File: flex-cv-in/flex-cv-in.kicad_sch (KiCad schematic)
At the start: 19 parts, among them J1 3.5mm_Mono_Switched, J2 HDR, U1 TLV9061xDBV

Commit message: Update to final Rev. A
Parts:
- added TP1: TP_VREF, TestPoint:TestPoint_Loop_D2.50mm_Drill1.0mm_LowProfile, symbol Connector:TestPoint
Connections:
- net VREF_1.65V: now also TP1.1
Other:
- moved on the sheet: C1, C2, C4, R5, R6

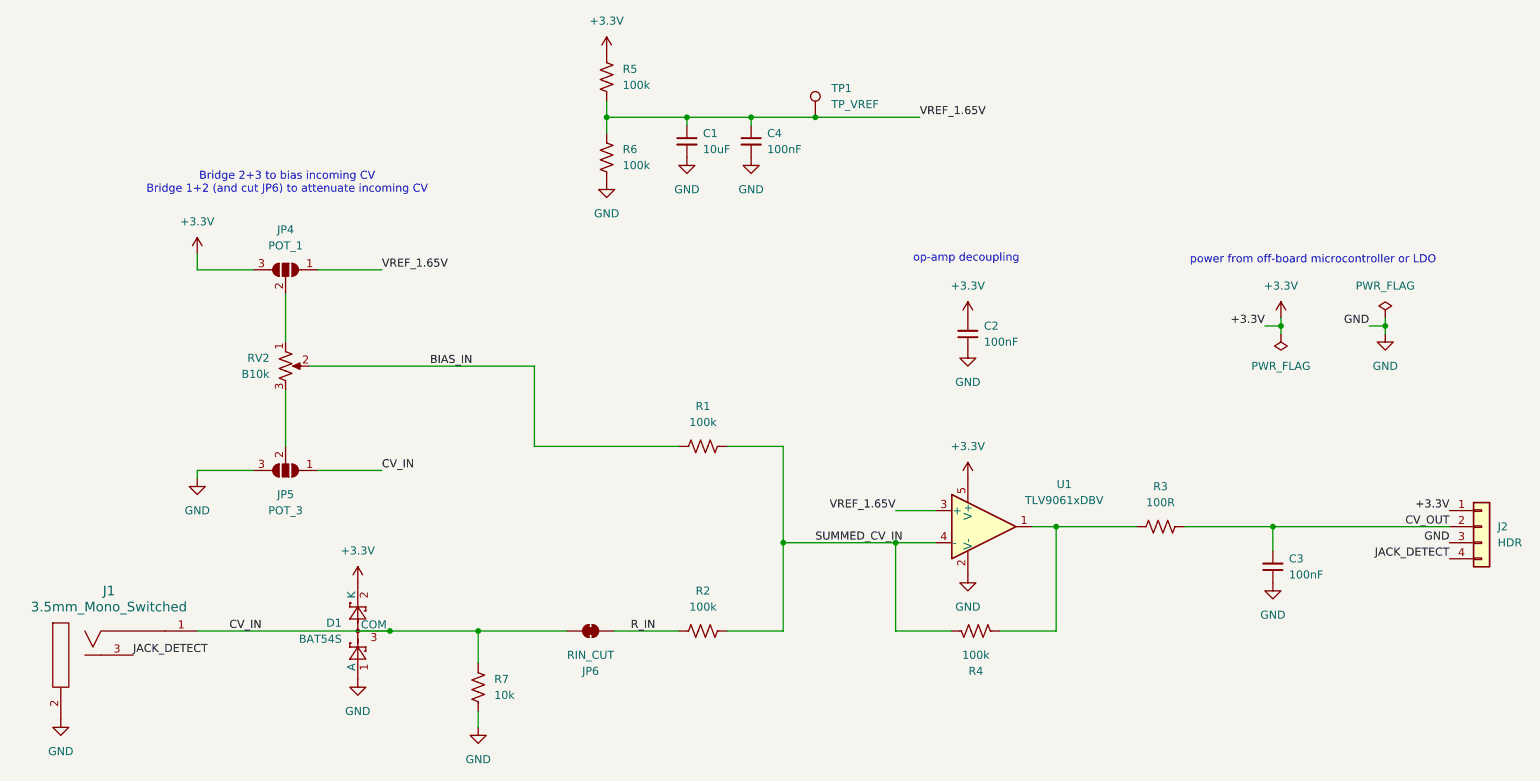
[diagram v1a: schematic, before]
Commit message: flex-cv-in rev. B
Updates and bug fixes:

- Removed jack detect
- Changed R7 connection from GND to VREF_1.65V
- Connected JP5 pad 2 to RV2 pad 3
- Adjusted layout of JP6 to avoid inadvertently cutting CV_IN trace
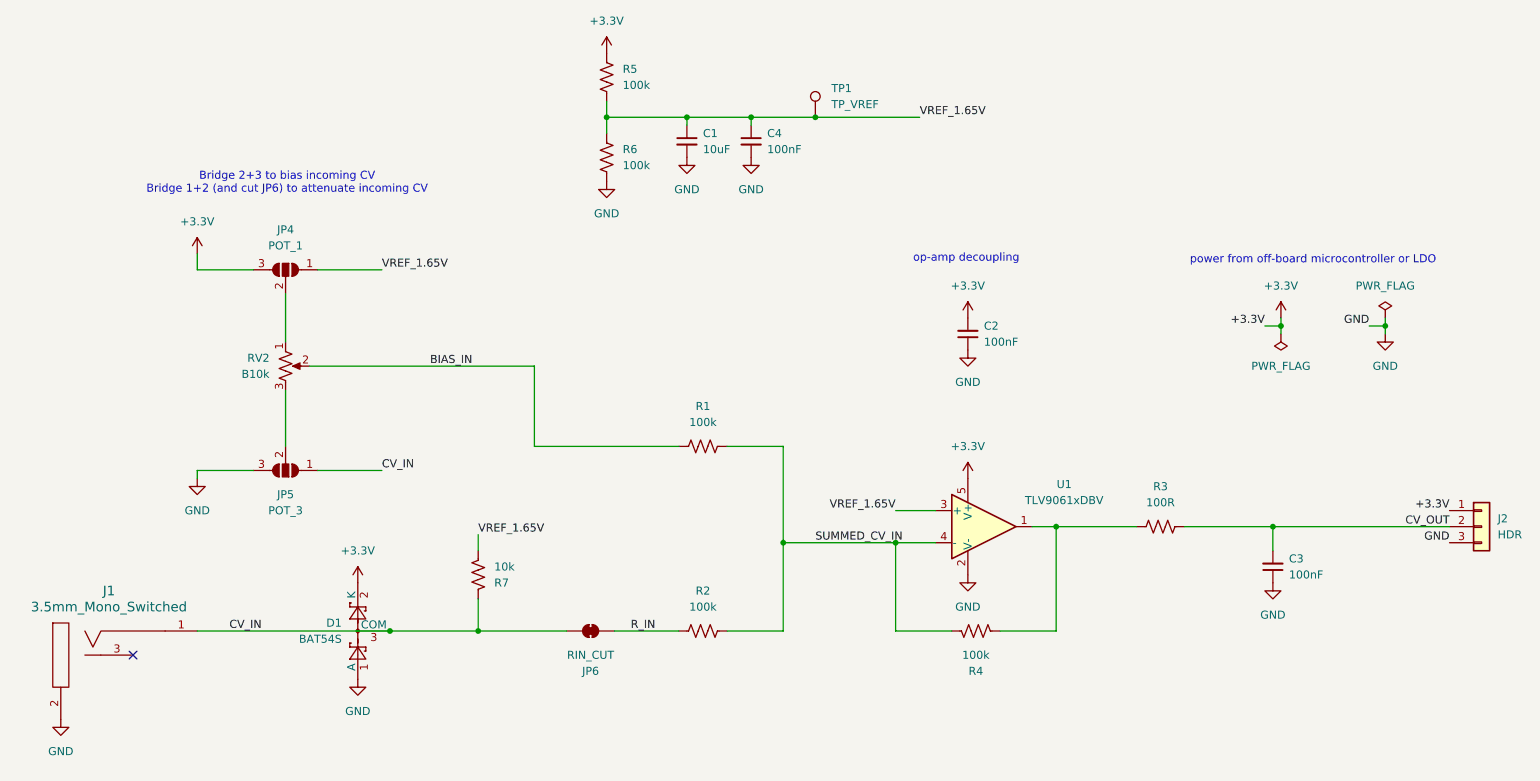
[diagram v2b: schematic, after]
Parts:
- removed J2: HDR, Connector_PinHeader_2.54mm:PinHeader_1x04_P2.54mm_Vertical, symbol Connector_Generic:Conn_01x04
- added J2: HDR, Connector_PinSocket_2.54mm:PinSocket_1x03_P2.54mm_Vertical, symbol Connector_Generic:Conn_01x03
- TP1: footprint TestPoint:TestPoint_Loop_D2.50mm_Drill1.0mm_LowProfile -> TestPoint:TestPoint_Pad_D1.5mm
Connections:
- net +3.3V: now also J2.1 (Pin_1)
- net CV_OUT: now also J2.2 (Pin_2)
- net GND: now also J2.3 (Pin_3); no longer R7.1
- net VREF_1.65V: now also R7.1
- net JACK_DETECT: no longer names the net of J1.3 (SW)
- no-connect marks 0 -> 1
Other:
- moved on the sheet: R7
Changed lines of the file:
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@@
 		(title "patch_bits/flex-cv-in")
 		(date "2025-07-18")
-		(rev "A")
+		(rev "B")
 		(company "Brian Varren")
 	)
@@
 		(color 0 0 0 0)
 	)
+	(no_connect
+		(at 59.69 121.92)
+	)
 	(wire
 		(pts
@@
 	(wire
 		(pts
-			(xy 114.3 130.81) (xy 114.3 133.35)
+			(xy 114.3 105.41) (xy 114.3 102.87)
 		)
 		(stroke
@@
 	(wire
 		(pts
-			(xy 114.3 118.11) (xy 114.3 123.19)
+			(xy 114.3 118.11) (xy 114.3 113.03)
 		)
 		(stroke
@@
 		)
 	)
-	(label "JACK_DETECT"
-		(at 267.97 106.68 180)
-		(effects
-			(font
-				(size 1.27 1.27)
-			)
-			(justify right bottom)
-		)
-	)
 	(label "GND"
 		(at 267.97 104.14 180)
@@
 		)
 	)
+	(label "VREF_1.65V"
+		(at 114.3 102.87 0)
+		(effects
+			(font
+				(size 1.27 1.27)
+			)
+			(justify left bottom)
+		)
+	)
 	(label "GND"
 		(at 255.27 69.85 180)
@@
 		)
 	)
-	(label "JACK_DETECT"
-		(at 59.69 121.92 0)
-		(effects
-			(font
-				(size 1.27 1.27)
-			)
-			(justify left bottom)
-		)
-	)
 	(label "CV_IN"
 		(at 99.06 92.71 0)
@@
 			)
 		)
-		(property "Footprint" "TestPoint:TestPoint_Loop_D2.50mm_Drill1.0mm_LowProfile"
+		(property "Footprint" "TestPoint:TestPoint_Pad_D1.5mm"
 			(at 172.72 36.83 0)
 			(effects
@@
 	(symbol
 		(lib_id "Device:R_US")
-		(at 114.3 127 180)
-		(unit 1)
-		(exclude_from_sim no)
-		(in_bom yes)
-		(on_board yes)
-		(dnp no)
-		(fields_autoplaced yes)
+		(at 114.3 109.22 0)
+		(mirror y)
+		(unit 1)
+		(exclude_from_sim no)
+		(in_bom yes)
+		(on_board yes)
+		(dnp no)
 		(property "Reference" "R7"
-			(at 116.84 125.7299 0)
+			(at 116.84 110.4901 0)
 			(effects
 				(font
@@
 		)
 		(property "Value" "10k"
-			(at 116.84 128.2699 0)
+			(at 116.84 107.9501 0)
 			(effects
 				(font
@@
 		)
 		(property "Footprint" "Resistor_SMD:R_0805_2012Metric"
-			(at 113.284 126.746 90)
+			(at 113.284 109.474 90)
 			(effects
 				(font
@@
 		)
 		(property "Datasheet" "~"
-			(at 114.3 127 0)
+			(at 114.3 109.22 0)
 			(effects
 				(font
@@
 		)
 		(property "Description" "Resistor, US symbol"
-			(at 114.3 127 0)
+			(at 114.3 109.22 0)
 			(effects
 				(font
@@
 	(symbol
 		(lib_id "power:GND")
-		(at 114.3 133.35 0)
-		(unit 1)
-		(exclude_from_sim no)
-		(in_bom yes)
-		(on_board yes)
-		(dnp no)
-		(fields_autoplaced yes)
-		(property "Reference" "#PWR04"
-			(at 114.3 139.7 0)
-			(effects
-				(font
-					(size 1.27 1.27)
-				)
-				(hide yes)
-			)
-		)
-		(property "Value" "GND"
-			(at 114.3 138.43 0)
-			(effects
-				(font
-					(size 1.27 1.27)
-				)
-			)
-		)
-		(property "Footprint" ""
-			(at 114.3 133.35 0)
-			(effects
-				(font
-					(size 1.27 1.27)
-				)
-				(hide yes)
-			)
-		)
-		(property "Datasheet" ""
-			(at 114.3 133.35 0)
-			(effects
-				(font
-					(size 1.27 1.27)
-				)
-				(hide yes)
-			)
-		)
-		(property "Description" "Power symbol creates a global label with name \"GND\" , ground"
-			(at 114.3 133.35 0)
-			(effects
-				(font
-					(size 1.27 1.27)
-				)
-				(hide yes)
-			)
-		)
-		(pin "1"
-		)
-		(instances
-			(project ""
-				(path "/9d06852e-8604-41db-99eb-9a7a414e7408"
-					(reference "#PWR04")
-					(unit 1)
-				)
-			)
-		)
-	)
-	(symbol
-		(lib_id "power:GND")
 		(at 157.48 43.18 0)
 		(unit 1)
@@
 	)
 	(symbol
-		(lib_id "Connector_Generic:Conn_01x04")
-		(at 273.05 101.6 0)
-		(unit 1)
-		(exclude_from_sim no)
-		(in_bom yes)
-		(on_board yes)
-		(dnp no)
-		(fields_autoplaced yes)
-		(property "Reference" "J2"
-			(at 275.59 101.5999 0)
-			(effects
-				(font
-					(size 1.27 1.27)
-				)
-				(justify left)
-			)
-		)
-		(property "Value" "HDR"
-			(at 275.59 104.1399 0)
-			(effects
-				(font
-					(size 1.27 1.27)
-				)
-				(justify left)
-			)
-		)
-		(property "Footprint" "Connector_PinHeader_2.54mm:PinHeader_1x04_P2.54mm_Vertical"
-			(at 273.05 101.6 0)
-			(effects
-				(font
-					(size 1.27 1.27)
-				)
-				(hide yes)
-			)
-		)
-		(property "Datasheet" "~"
-			(at 273.05 101.6 0)
-			(effects
-				(font
-					(size 1.27 1.27)
-				)
-				(hide yes)
-			)
-		)
-		(property "Description" "Generic connector, single row, 01x04, script generated (kicad-library-utils/schlib/autogen/connector/)"
-			(at 273.05 101.6 0)
-			(effects
-				(font
-					(size 1.27 1.27)
-				)
-				(hide yes)
-			)
-		)
-		(pin "1"
-		)
-		(pin "4"
-		)
-		(pin "2"
-		)
-		(pin "3"
-		)
-		(instances
-			(project "biased-CV-input-unity"
-				(path "/9d06852e-8604-41db-99eb-9a7a414e7408"
-					(reference "J2")
-					(unit 1)
-				)
-			)
-		)
-	)
-	(symbol
 		(lib_id "power:+3.3V")
 		(at 69.85 58.42 0)
@@
 					(unit 1)
 				)
+			)
+		)
+	)
+	(symbol
+		(lib_id "Connector_Generic:Conn_01x03")
+		(at 273.05 101.6 0)
+		(unit 1)
+		(exclude_from_sim no)
+		(in_bom yes)
+		(on_board yes)
+		(dnp no)
+		(fields_autoplaced yes)
+		(property "Reference" "J2"
+			(at 275.59 100.3299 0)
+			(effects
+				(font
+					(size 1.27 1.27)
+				)
+				(justify left)
+			)
+		)
+		(property "Value" "HDR"
+			(at 275.59 102.8699 0)
+			(effects
+				(font
+					(size 1.27 1.27)
+				)
+				(justify left)
+			)
+		)
+		(property "Footprint" "Connector_PinSocket_2.54mm:PinSocket_1x03_P2.54mm_Vertical"
+			(at 273.05 101.6 0)
+			(effects
+				(font
+					(size 1.27 1.27)
+				)
+				(hide yes)
+			)
+		)
+		(property "Datasheet" "~"
+			(at 273.05 101.6 0)
+			(effects
+				(font
+					(size 1.27 1.27)
+				)
+				(hide yes)
+			)
+		)
+		(property "Description" "Generic connector, single row, 01x03, script generated (kicad-library-utils/schlib/autogen/connector/)"
+			(at 273.05 101.6 0)
+			(effects
+				(font
+					(size 1.27 1.27)
+				)
+				(hide yes)
+			)
+		)
+		(pin "1"
+		)
+		(pin "3"
+		)
+		(pin "2"
+		)
+		(instances
+			(project ""
+				(path "/9d06852e-8604-41db-99eb-9a7a414e7408"
+					(reference "J2")
+					(unit 1)
+				)
